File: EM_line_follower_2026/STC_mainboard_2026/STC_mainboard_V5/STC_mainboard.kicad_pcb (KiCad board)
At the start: 2 copper layers, 85 x 78.2 mm, 111 parts, among them J1 Conn_01x04, J10 Conn_01x04, J11 WirePad, J12 WirePad, J15 WirePad, J16 WirePad, J2 WirePad, J20 WirePad, J21 WirePad, J3 WirePad, J4 Conn_01x02, J5 WirePad, J6 WirePad, J7 WirePad, J8 WirePad, J9 WirePad, P1 VALUE, P2 VALUE, SW1 SW_Push, SW3 SW_Push, U1 STC16H40K128_CoreBoard, U11 TPS54360DDA, U3 LSM6DSRTR, U4 LM1117-3.3V, U5 OPA2197xD, U6 OPA2197xD, U7 OPA2197xD

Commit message: upload intern pcb
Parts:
- removed C10: 10V 1000uF, HKUST_RDC2025_Footprint_Lib:CP_Radial_D8.0mm_P12.00mm
- removed the G*** at (28.8, 33.2)
- removed R3: 0R, HKUST_RDC2025_Footprint_Lib:R_0603_1608Metric
- moved C6 72.1 mm to (21.0, 26.8), turned to 45 degrees
- moved C5 71.8 mm to (19.5, 25.5), turned to 45 degrees
- moved C8 63.4 mm to (14.1, 26.5)
- moved C7 59.2 mm to (9.40, 22.8), turned to 90 degrees
- moved R1 53.5 mm to (11.7, 19.0)
- moved R4 52.7 mm to (15.6, 18.5)
- moved C9 51.0 mm to (8.90, 16.0), turned to 90 degrees
- moved R2 50.0 mm to (8.90, 19.3), turned to -90 degrees
- moved L1 46.6 mm to (14.3, 13.0)
- moved D2 33.1 mm to (13.4, 7.00)
- moved U11 24.4 mm to (14.5, 22.5)
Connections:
- C9 pad 1: Net-(C10-Pad1) -> +5V
- L1 pad 2: Net-(C10-Pad1) -> +5V
- R1 pad 2: Net-(C10-Pad1) -> +5V
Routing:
- net +5V: track 285.7 -> 324.8 mm
- net Net-(D2-K): track 0.00 -> 28.4 mm
- net /P3.4: track 34.0 -> 41.0 mm
- net /P5.0: track 30.9 -> 36.7 mm
- net /FB: track 0.00 -> 4.52 mm
- net Net-(U11-BOOT): track 0.00 -> 3.31 mm
- net Net-(U11-RT/CLK): track 0.00 -> 2.11 mm
- net Net-(U11-COMP): track 0.00 -> 2.08 mm
- net /P3.5: track 31.2 -> 31.9 mm
- net +12V: track 125.0 -> 125.7 mm
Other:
- outline, holes or cut-outs redrawn

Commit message: modify STM mainboard V5
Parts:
- removed C29: 47uF, HKUST_RDC2024_Footprint_Lib:C_0603_1608Metric
- removed D17: MM3Zxx, Diode_SMD:D_SOD-323F
- removed G*** (x2): LOGO, LOGO
- removed J15, J16: WirePad, China5.0:WirePad_motor
- removed J4: Conn_01x02, Connector_JST:JST_XH_B2B-XH-A_1x02_P2.50mm_Vertical
- removed R53: 1k, HKUST_RDC2024_Footprint_Lib:R_0603_1608Metric
- removed U11: TPS54360DDA, HKUST_RDC2025_Footprint_Lib:SOIC-8_3.9x4.9mm_P1.27mm
- added 1: ~, ProLib_1pcs_2026-06-16.elibz:BT2.0, F.Cu at (127.0, 125.5)
- added 11: ~, ProLib_1pcs_2026-06-16.elibz:BT2.0, F.Cu at (127.0, 130.0)
- added 111: ~, ProLib_1pcs_2026-06-16.elibz:BT2.0, F.Cu at (127.0, 134.4)
- added C10: 1000uF, Capacitor_SMD:CP_Elec_4x5.3, F.Cu at (184.8, 105.7)
- added C2: 47uF, HKUST_RDC2024_Footprint_Lib:C_0603_1608Metric, F.Cu at (216.0, 97.6)
- added D1: SS54, HKUST_RDC2024_Footprint_Lib:D_SMA, F.Cu at (193.5, 98.4)
- added J23: WirePad, China5.0:WirePad_motor, F.Cu at (219.8, 97.5)
- added J24: WirePad, China5.0:WirePad_motor, F.Cu at (219.8, 99.8)
- added R3: 10.2k, HKUST_RDC2024_Footprint_Lib:R_0603_1608Metric, F.Cu at (178.9, 106.1)
- added R5: 1k, HKUST_RDC2024_Footprint_Lib:R_0603_1608Metric, F.Cu at (74.3, 136.3)
- added U2: ~, Package_SO:SOIC-8-1EP_3.9x4.9mm_P1.27mm_EP2.29x3mm, F.Cu at (71.4, 131.0)
- C11, C13, C26, C33, C4, C51, C52, D19, D21, D22, D24, J20, J21, R11, R17, R20, R59, R60, U3, U8, U9: moved to F.Cu
- C5, C6, C9: footprint HKUST_RDC2025_Footprint_Lib:C_0603_1608Metric -> HKUST_RDC2024_Footprint_Lib:C_0603_1608Metric
- C7: value 39pF -> 100nF; footprint HKUST_RDC2025_Footprint_Lib:C_0603_1608Metric -> HKUST_RDC2024_Footprint_Lib:C_0603_1608Metric
- C8: value 100nF -> 39F; footprint HKUST_RDC2025_Footprint_Lib:C_0603_1608Metric -> HKUST_RDC2024_Footprint_Lib:C_0603_1608Metric
- D2: value SS54 -> MM3Zxx; footprint HKUST_RDC2025_Footprint_Lib:D_SMA -> Diode_SMD:D_SOD-323F
- L1: footprint HKUST_RDC2025_Footprint_Lib:L_7.3x7.3_H3.5 -> HKUST_RDC2024_Footprint_Lib:L_7.3x7.3_H3.5
- R1: value 53.6k -> 162k; footprint HKUST_RDC2025_Footprint_Lib:R_0603_1608Metric -> HKUST_RDC2024_Footprint_Lib:R_0603_1608Metric
- R2: value 10.2k -> 53.6k; footprint HKUST_RDC2025_Footprint_Lib:R_0603_1608Metric -> HKUST_RDC2024_Footprint_Lib:R_0603_1608Metric
- R4: value 162k -> 0R; footprint HKUST_RDC2025_Footprint_Lib:R_0603_1608Metric -> HKUST_RDC2024_Footprint_Lib:R_0603_1608Metric
- U10: value ~ -> TPS54360DDA; footprint Package_SO:SOIC-8-1EP_3.9x4.9mm_P1.27mm_EP2.29x3mm -> Package_SO:TI_SO-PowerPAD-8_ThermalVias; moved to F.Cu
- moved J1 235.3 mm to (50.7, 201.9), turned to 0 degrees
- moved J6 225.8 mm to (52.9, 197.1)
- moved C31 223.7 mm to (52.9, 193.9), turned to -90 degrees
- moved J5 223.4 mm to (58.8, 192.1), turned to -90 degrees
- moved U1 220.9 mm to (89.8, 192.2), turned to 90 degrees
- moved C25 220.8 mm to (58.8, 189.1), turned to -90 degrees
- moved D11 219.8 mm to (51.8, 191.3), turned to 180 degrees
- moved D9 219.2 mm to (57.7, 186.6), turned to 180 degrees
- moved D18 217.7 mm to (52.9, 188.5), turned to -90 degrees
- moved C21 217.1 mm to (75.9, 178.2)
- moved R24 216.3 mm to (73.6, 178.9), turned to 0 degrees
- moved D10 215.0 mm to (66.1, 183.9), turned to -90 degrees
- moved R27 214.6 mm to (63.7, 181.4)
- moved R28 214.3 mm to (52.0, 185.9), turned to 180 degrees
- moved U5 213.6 mm to (58.4, 180.8), turned to 180 degrees
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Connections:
- C5 pad 1: GND -> +12V
- C5 pad 2: +12V -> GND
- C6 pad 1: GND -> +12V
- C6 pad 2: +12V -> GND
- C7 pad 1: GND -> Net-(U10-BOOT)
- C7 pad 2: Net-(U11-COMP) -> Net-(D1-K)
- C8 pad 1: Net-(D2-K) -> Net-(U10-COMP)
- C8 pad 2: Net-(U11-BOOT) -> GND
- C9 pad 1: +5V -> Net-(C10-Pad1)
- L1 pad 1: Net-(D2-K) -> Net-(D1-K)
- L1 pad 2: +5V -> Net-(C10-Pad1)
- R1 pad 1: /FB -> Net-(U10-RT/CLK)
- R1 pad 2: +5V -> GND
- R2 pad 1: GND -> Net-(C10-Pad1)
- R4 pad 1: GND -> Net-(C10-Pad1)
- R4 pad 2: Net-(U11-RT/CLK) -> +5V
- U10 pad 1: GND -> Net-(U10-BOOT)
- U10 pad 2: /P7.6 -> +12V
- U10 pad 3: /P7.4 -> unconnected-(U10-EN-Pad3)
- U10 pad 4: Net-(D17-K) -> Net-(U10-RT/CLK)
- U10 pad 5: +12V -> /FB
- U10 pad 6: /fan1 -> Net-(U10-COMP)
- U10 pad 8: /fan2 -> Net-(D1-K)
- U8 pad 2: /P6.2 -> /P6.0
- U8 pad 3: /P6.0 -> /P6.2
- U9 pad 2: /P6.6 -> /P6.4
- U9 pad 3: /P6.4 -> /P6.6
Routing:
- net +5V: track 324.8 -> 0.00 mm, vias 3 -> 0
- net +12V: track 125.7 -> 26.1 mm, vias 10 -> 0
- net /P6.0: track 18.0 -> 111.7 mm
- net /P6.6: track 7.17 -> 69.1 mm
- net /P6.4: track 7.83 -> 69.7 mm
- net /P6.2: track 18.6 -> 78.6 mm
- net Net-(R24-Pad1): track 51.4 -> 16.9 mm
- net Net-(D2-K): track 28.4 -> 5.03 mm
- net /P4.0: track 38.5 -> 15.3 mm, vias 2 -> 0
- net /P5.3: track 7.03 -> 27.4 mm
- net Net-(R25-Pad1): track 60.5 -> 41.2 mm
- net /P3.6: track 16.4 -> 0.00 mm, vias 1 -> 0
- net +3.3V: track 20.4 -> 4.51 mm, vias 1 -> 0
- net /P6.3: track 15.8 -> 0.00 mm
- net /P5.2: track 7.04 -> 21.9 mm
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- removed copper zone on B.Cu, net +12V
- removed copper zone on F.Cu, net +12V
- removed copper zone on B.Cu, net GND
- removed copper zone on F.Cu, net GND
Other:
- board size 85 x 78.2 mm -> 105 x 94.1 mm
- board text removed: "${REFERENCE}"
- board text removed: "L1"
- board text removed: "L2"
- board text removed: "L3"
- board text removed: "L4"
- board text removed: "L5"

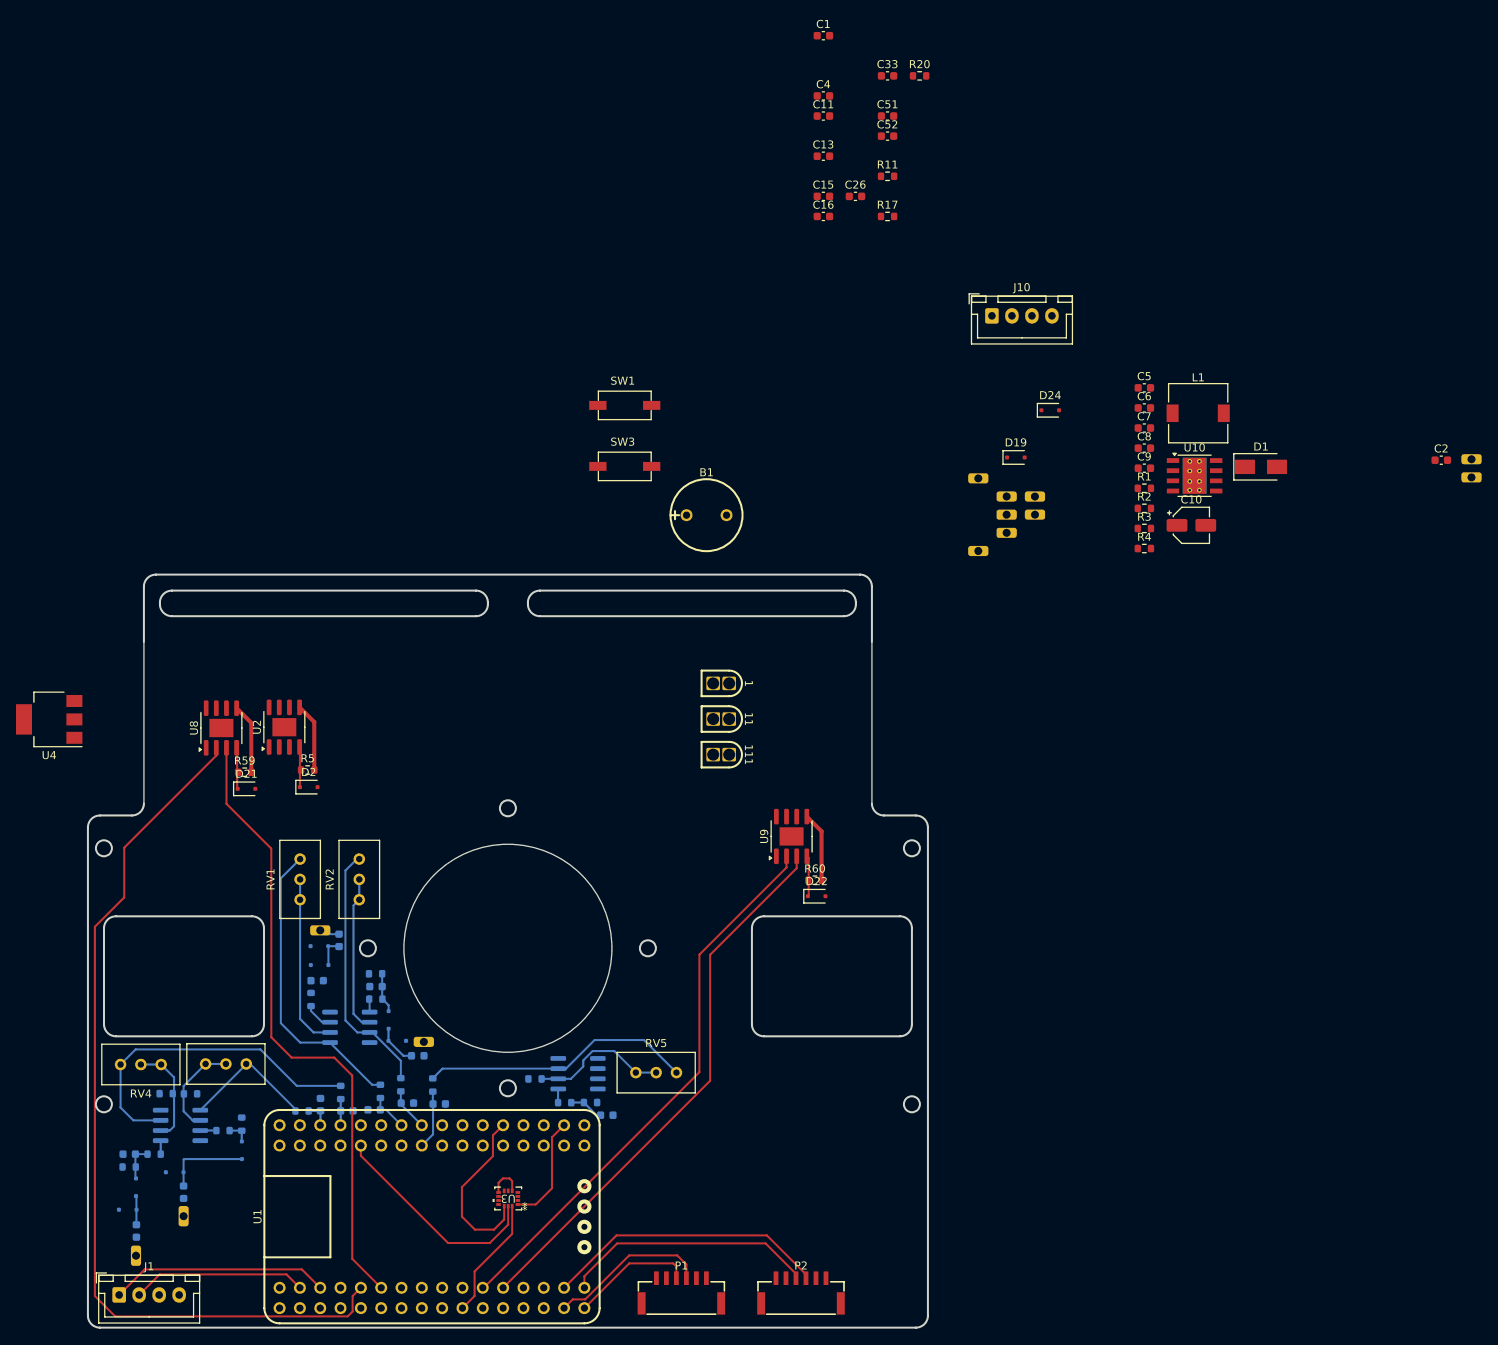
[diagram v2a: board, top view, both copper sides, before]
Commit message: first draft for V5 need to redraw the buzzer footprint and reduce the length of the board
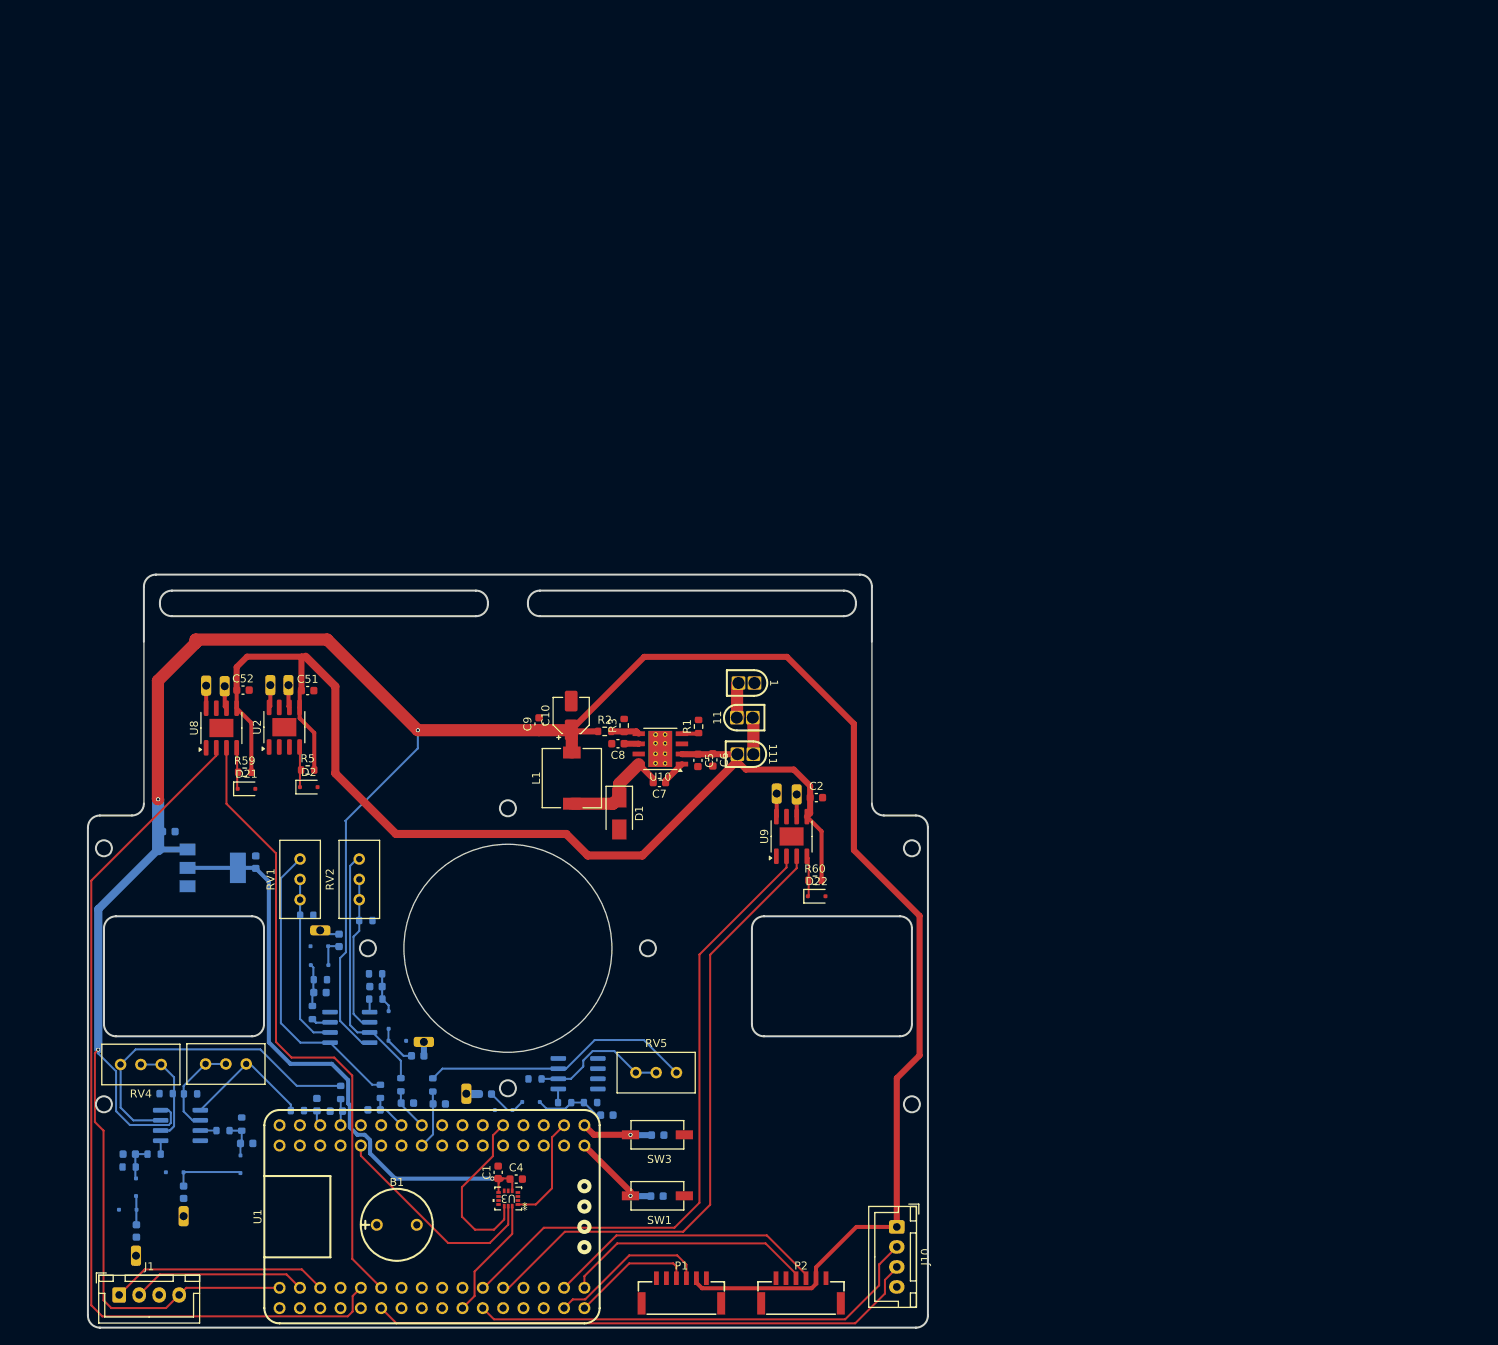
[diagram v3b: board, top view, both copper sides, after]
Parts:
- removed J12, J9: WirePad, China5.0:WirePad_motor
- removed R4: 0R, HKUST_RDC2024_Footprint_Lib:R_0603_1608Metric
- C11, C13, C15, C16, C26, C33, D19, D24, R11, R17, R20, U4: moved to B.Cu
- moved J23 152.7 mm to (69.7, 125.8), turned to 90 degrees
- moved J24 150.1 mm to (72.0, 125.8), turned to 90 degrees
- moved C1 147.8 mm to (98.1, 186.6), turned to 90 degrees
- moved C26 140.7 mm to (66.7, 183.0)
- moved C4 140.7 mm to (100.4, 187.5)
- moved C33 136.8 mm to (96.5, 176.8), turned to 180 degrees
- moved C11 136.6 mm to (118.0, 189.6), turned to 180 degrees
- moved R20 126.3 mm to (81.6, 155.1), turned to 180 degrees
- moved C13 124.1 mm to (118.1, 182.0), turned to 180 degrees
- moved R11 122.9 mm to (75.9, 162.5)
- moved J10 114.5 mm to (147.9, 193.4), turned to -90 degrees
- moved C15 114.0 mm to (57.0, 144.0)
- moved R17 113.6 mm to (74.2, 154.5), turned to 180 degrees
- moved D24 108.1 mm to (102.2, 177.8), turned to 180 degrees
- moved C16 107.5 mm to (67.8, 147.8), turned to 90 degrees
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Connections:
- C10 pad 1: Net-(C10-Pad1) -> +5V
- C9 pad 1: Net-(C10-Pad1) -> +5V
- L1 pad 2: Net-(C10-Pad1) -> +5V
- R2 pad 1: Net-(C10-Pad1) -> +5V
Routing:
- net +5V: track 0.00 -> 377.9 mm, vias 0 -> 3
- net +12V: track 26.1 -> 145.2 mm
- net +3.3V: track 4.51 -> 76.0 mm, vias 0 -> 1
- net /P6.3: track 0.00 -> 69.2 mm
- net /P6.5: track 0.00 -> 57.6 mm
- net Net-(D1-K): track 0.00 -> 14.5 mm
- net /P3.7: track 0.00 -> 11.2 mm, vias 0 -> 1
- net /P6.4: track 69.7 -> 79.3 mm
- net /P6.6: track 69.1 -> 78.2 mm
- net /P3.6: track 0.00 -> 8.90 mm, vias 0 -> 1
- net Net-(D6-K): track 0.00 -> 5.30 mm
- net Net-(D19-K): track 0.00 -> 5.08 mm
- net Net-(11-+): track 0.00 -> 4.60 mm
- net Net-(D24-K): track 4.33 -> 8.93 mm
- net Net-(1-+): track 0.00 -> 4.56 mm
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
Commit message: finish the V5 design
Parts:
- removed P1, P2: VALUE, 2K0300久久派_主板_V1.0:ECD-GH1.25-6P-SH
- added J12: WirePad, STC_mainboard_lib:WirePad_motor, F.Cu at (91.7, 187.4)
- added J13: Conn_01x02, Connector_AMASS:AMASS_XT30U-M_1x02_P5.0mm_Vertical, F.Cu at (126.0, 142.3)
- added J14: WirePad, STC_mainboard_lib:WirePad_motor, F.Cu at (67.9, 152.5)
- added J15: WirePad, STC_mainboard_lib:WirePad_motor, F.Cu at (82.0, 172.4)
- added J16: WirePad, STC_mainboard_lib:WirePad_motor, F.Cu at (101.8, 172.6)
- added J4: Conn_01x04, Connector_JST:JST_GH_BM04B-GHS-TBT_1x04-1MP_P1.25mm_Vertical, F.Cu at (122.2, 201.4)
- added J9: Conn_01x04, Connector_JST:JST_GH_BM04B-GHS-TBT_1x04-1MP_P1.25mm_Vertical, F.Cu at (137.1, 201.4)
- B1: footprint 龙芯LS2K0300主板V2.0:BEEP 9x5.5mm -> Inductor_SMD:L_12x12mm_H4.5mm
- moved 1 23.8 mm to (129.3, 149.2), turned to 180 degrees
- moved 111 17.6 mm to (120.4, 149.1), turned to 180 degrees
- moved 11 17.5 mm to (125.0, 147.0), turned to 0 degrees
- moved R5 4.76 mm to (74.3, 141.1)
- moved R59 4.76 mm to (66.4, 141.4)
- moved U8 4.76 mm to (63.5, 135.8)
- moved J11 4.76 mm to (64.0, 130.6)
- moved C51 4.75 mm to (74.3, 131.2)
- moved C52 4.75 mm to (66.2, 131.1)
- moved D2 4.75 mm to (74.4, 143.2)
- moved D21 4.75 mm to (66.7, 143.4)
- moved J7 4.75 mm to (61.7, 130.6)
- moved U2 4.75 mm to (71.4, 135.7)
- moved J23 4.75 mm to (69.7, 130.5)
- moved J24 4.75 mm to (72.0, 130.5)
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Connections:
- U2 pad 2: /P7.4 -> /P7.6
- U2 pad 3: /P7.6 -> /P7.4
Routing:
- net /P7.4: track 0.00 -> 55.8 mm
- net /P7.6: track 0.00 -> 54.4 mm
- net +3.3V: track 76.0 -> 23.7 mm
- net +5V: track 377.9 -> 353.5 mm
- net /P1.7: track 0.00 -> 12.7 mm
- net +12V: track 145.2 -> 139.4 mm
- net Net-(1-+): track 4.56 -> 0.00 mm
- net /P6.2: track 78.6 -> 82.5 mm
- net /L3: track 0.00 -> 2.34 mm
- net /P6.0: track 113.0 -> 110.8 mm
- net /L1: track 0.00 -> 2.22 mm
- net /P4.3: track 27.5 -> 25.6 mm
- net /P3.4: track 35.4 -> 37.0 mm
- net /P5.0: track 31.7 -> 32.4 mm
- net /P6.6: track 78.2 -> 77.6 mm
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- added copper zone on B.Cu, net +5V
- added copper zone on F.Cu, net GND
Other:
- board size 105 x 94.1 mm -> 105 x 86.5 mm
